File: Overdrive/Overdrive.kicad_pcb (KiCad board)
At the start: 2 copper layers, 85 x 86 mm, 53 parts, among them J1 Stereo In, J2 Barrel_Jack_Switch, J3 Mono Out, J4 M2, J5 M2, J6 M2, J7 M2, Q1 2N2222, Q2 2N2222, SW1 Footswitch, U1 RC4558

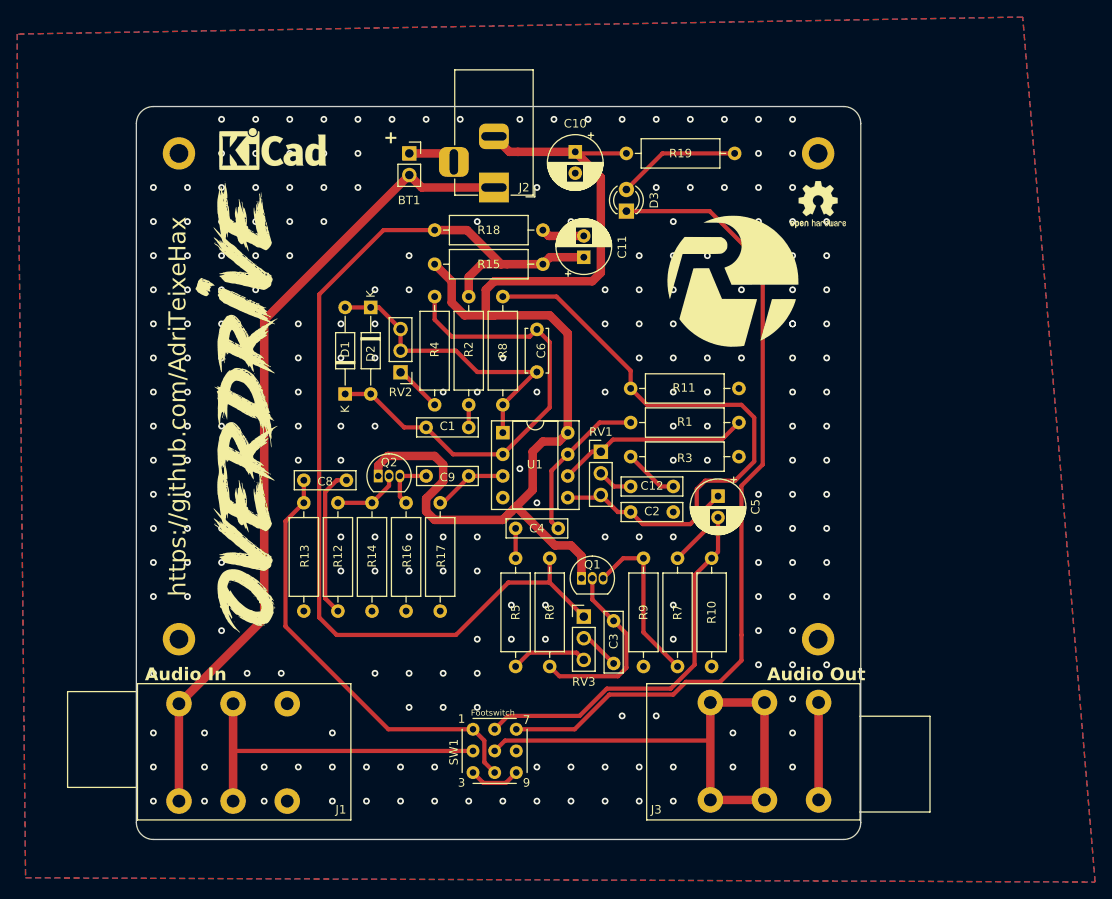
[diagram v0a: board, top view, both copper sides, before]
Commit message: Redesigned board to fit 125B case
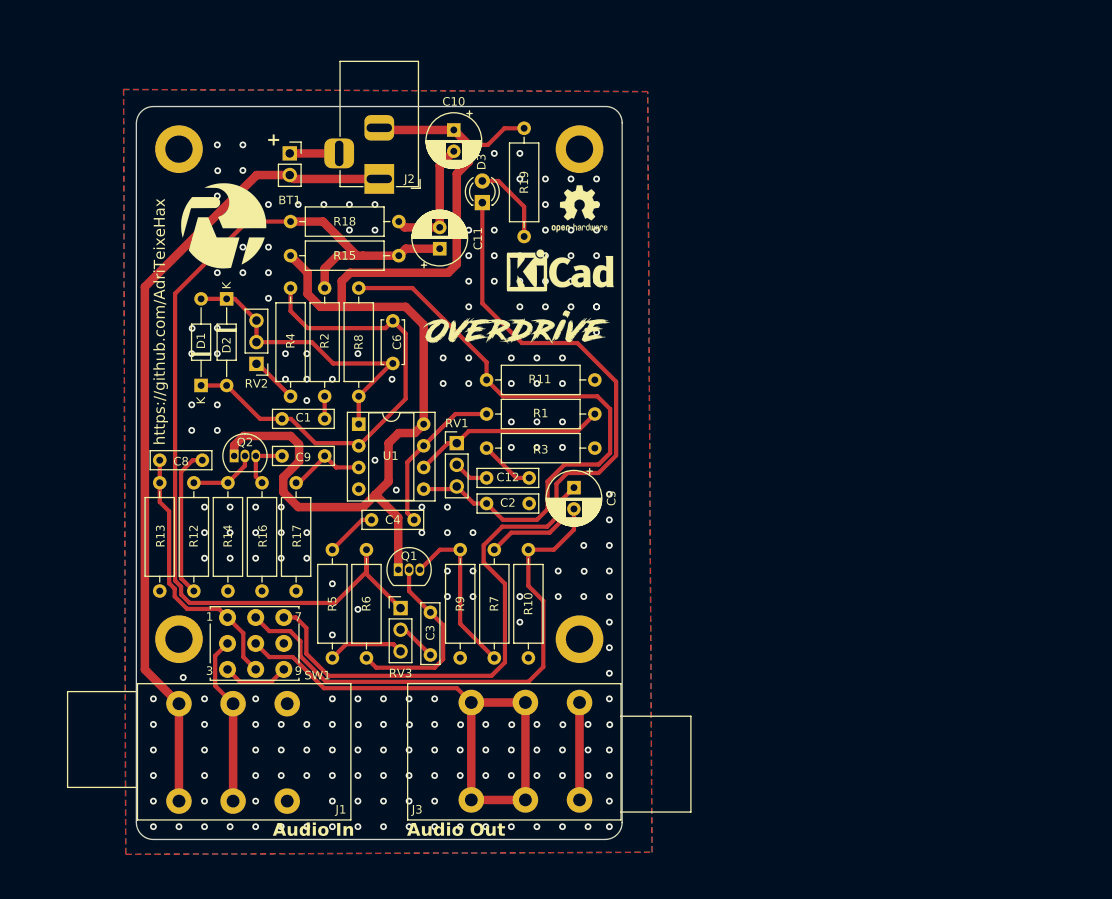
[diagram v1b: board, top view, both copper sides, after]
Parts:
- removed the G*** at (159.0, 88.0)
- removed the G*** at (104.0, 103.0)
- added G***: LOGO, LOGO, F.Cu at (99.2, 81.5)
- added G***: LOGO, LOGO, F.Cu at (133.5, 94.8)
- J4, J5, J6, J7: footprint MountingHole:MountingHole_2.2mm_M2_DIN965_Pad -> MountingHole:MountingHole_3.2mm_M3_DIN965_Pad
- moved REF** 36.6 mm to (138.8, 87.2)
- moved SW1 31.6 mm to (99.7, 127.5)
- moved J3 28.0 mm to (128.3, 137.4)
- moved J5 28.0 mm to (141.0, 72.5)
- moved REF** 28.0 mm to (141.0, 79.5)
- moved J7 28.0 mm to (141.0, 130.0)
- moved R19 26.6 mm to (134.5, 82.8), turned to 90 degrees
- moved C3 21.5 mm to (123.5, 131.8)
- moved R10 21.5 mm to (135.0, 119.5)
- moved R5 21.5 mm to (112.0, 119.5)
- moved R6 21.5 mm to (116.0, 132.2)
- moved R7 21.5 mm to (131.0, 132.2)
- moved R9 21.5 mm to (127.0, 119.5)
- moved RV3 21.5 mm to (120.0, 126.3)
- moved Q1 21.5 mm to (119.7, 121.8)
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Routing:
- net Net-(J1-PadR): track 45.1 -> 20.0 mm
- net Net-(C8-Pad1): track 51.2 -> 31.4 mm
- net Net-(C5-Pad2): track 45.0 -> 61.9 mm
- net Net-(D3-K): track 95.9 -> 108.2 mm
- net GND: track 16.5 -> 26.1 mm, vias 231 -> 216
- net +4V: track 119.7 -> 113.6 mm
- net Net-(D3-A): track 14.5 -> 9.65 mm
- net Net-(J3-PadR): track 68.3 -> 63.7 mm
- net Net-(C5-Pad1): track 9.25 -> 13.8 mm
- net +9V: track 137.1 -> 133.5 mm
- net Net-(C4-Pad2): track 3.50 -> 6.04 mm
- net Net-(SW1-Pad3): track 6.08 -> 7.81 mm
- net Net-(U1A-+): track 8.30 -> 9.36 mm
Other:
- board size 85 x 86 mm -> 57 x 86 mm

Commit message: added bom, gerber files and fixed last errors in pcb
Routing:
- net GND: track 26.1 -> 34.1 mm, vias 216 -> 225
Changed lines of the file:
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@@
       (outputformat 1)
       (mirror false)
-      (drillshape 1)
+      (drillshape 0)
       (scaleselection 1)
       (outputdirectory "")
@@
   (segment (start 130.095 99.58) (end 130.095 97.5) (width 0.5) (layer "F.Cu") (net 5))
   (segment (start 143.245 109.5) (end 144.595 108.15) (width 0.5) (layer "F.Cu") (net 5))
+  (segment (start 142.795 99.58) (end 139.42 99.58) (width 0.25) (layer "F.Cu") (net 6))
+  (segment (start 91.745 124.35) (end 91.745 120.745) (width 0.25) (layer "F.Cu") (net 6))
   (segment (start 126.25 72.75) (end 124.595 74.405) (width 1) (layer "F.Cu") (net 6))
+  (segment (start 91.745 120.745) (end 91.5 120.5) (width 0.25) (layer "F.Cu") (net 6))
   (segment (start 124.595 74.405) (end 124.595 81.682379) (width 1) (layer "F.Cu") (net 6))
   (segment (start 141 137.43) (end 141 148.86) (width 1) (layer "F.Cu") (net 6))
   (segment (start 120.477379 81.682379) (end 119.795 81) (width 1) (layer "F.Cu") (net 6))
+  (segment (start 139.42 99.58) (end 139 100) (width 0.25) (layer "F.Cu") (net 6))
   (segment (start 124.595 81.682379) (end 120.477379 81.682379) (width 1) (layer "F.Cu") (net 6))
   (via (at 124 137) (size 0.8) (drill 0.4) (layers "F.Cu" "B.Cu") (free) (net 6))
@@
   (via (at 124 149) (size 0.8) (drill 0.4) (layers "F.Cu" "B.Cu") (free) (net 6))
   (via (at 109 117.5) (size 0.8) (drill 0.4) (layers "F.Cu" "B.Cu") (free) (net 6))
+  (via (at 92.5 78) (size 0.8) (drill 0.4) (layers "F.Cu" "B.Cu") (free) (net 6))
   (via (at 138.5 122) (size 0.8) (drill 0.4) (layers "F.Cu" "B.Cu") (free) (net 6))
   (via (at 101.5 87) (size 0.8) (drill 0.4) (layers "F.Cu" "B.Cu") (free) (net 6))
@@
   (via (at 118 137) (size 0.8) (drill 0.4) (layers "F.Cu" "B.Cu") (free) (net 6))
   (via (at 139.045931 140.032175) (size 0.8) (drill 0.4) (layers "F.Cu" "B.Cu") (free) (net 6))
+  (via (at 108 69) (size 0.8) (drill 0.4) (layers "F.Cu" "B.Cu") (free) (net 6))
   (via (at 117 79) (size 0.8) (drill 0.4) (layers "F.Cu" "B.Cu") (free) (net 6))
   (via (at 91 137) (size 0.8) (drill 0.4) (layers "F.Cu" "B.Cu") (free) (net 6))
@@
   (via (at 115 152) (size 0.8) (drill 0.4) (layers "F.Cu" "B.Cu") (free) (net 6))
   (via (at 104.5 79) (size 0.8) (drill 0.4) (layers "F.Cu" "B.Cu") (free) (net 6))
-  (via (at 143 76) (size 0.8) (drill 0.4) (layers "F.Cu" "B.Cu") (free) (net 6))
+  (via (at 95.5 81) (size 0.8) (drill 0.4) (layers "F.Cu" "B.Cu") (free) (net 6))
   (via (at 112 149) (size 0.8) (drill 0.4) (layers "F.Cu" "B.Cu") (free) (net 6))
   (via (at 137 91) (size 0.8) (drill 0.4) (layers "F.Cu" "B.Cu") (free) (net 6))
   (via (at 144.5 146) (size 0.8) (drill 0.4) (layers "F.Cu" "B.Cu") (free) (net 6))
   (via (at 134 76) (size 0.8) (drill 0.4) (layers "F.Cu" "B.Cu") (free) (net 6))
+  (via (at 95.5 78) (size 0.8) (drill 0.4) (layers "F.Cu" "B.Cu") (free) (net 6))
   (via (at 103 152) (size 0.8) (drill 0.4) (layers "F.Cu" "B.Cu") (free) (net 6))
+  (via (at 91.5 120.5) (size 0.8) (drill 0.4) (layers "F.Cu" "B.Cu") (free) (net 6))
   (via (at 103 140) (size 0.8) (drill 0.4) (layers "F.Cu" "B.Cu") (free) (net 6))
   (via (at 133.045931 140.032175) (size 0.8) (drill 0.4) (layers "F.Cu" "B.Cu") (free) (net 6))
@@
   (via (at 144.5 122) (size 0.8) (drill 0.4) (layers "F.Cu" "B.Cu") (free) (net 6))
   (via (at 98.5 87) (size 0.8) (drill 0.4) (layers "F.Cu" "B.Cu") (free) (net 6))
+  (via (at 92.5 84) (size 0.8) (drill 0.4) (layers "F.Cu" "B.Cu") (free) (net 6))
   (via (at 127 143) (size 0.8) (drill 0.4) (layers "F.Cu" "B.Cu") (free) (net 6))
   (via (at 133 100) (size 0.8) (drill 0.4) (layers "F.Cu" "B.Cu") (free) (net 6))
@@
   (via (at 112 99.5) (size 0.8) (drill 0.4) (layers "F.Cu" "B.Cu") (free) (net 6))
   (via (at 109 152) (size 0.8) (drill 0.4) (layers "F.Cu" "B.Cu") (free) (net 6))
+  (via (at 101.5 69) (size 0.8) (drill 0.4) (layers "F.Cu" "B.Cu") (free) (net 6))
   (via (at 101.5 84) (size 0.8) (drill 0.4) (layers "F.Cu" "B.Cu") (free) (net 6))
   (via (at 127.045931 140.032175) (size 0.8) (drill 0.4) (layers "F.Cu" "B.Cu") (free) (net 6))
+  (via (at 111.5 69) (size 0.8) (drill 0.4) (layers "F.Cu" "B.Cu") (free) (net 6))
   (via (at 144.5 125) (size 0.8) (drill 0.4) (layers "F.Cu" "B.Cu") (free) (net 6))
   (via (at 133 107.5) (size 0.8) (drill 0.4) (layers "F.Cu" "B.Cu") (free) (net 6))
@@
   (via (at 95.5 105.5) (size 0.8) (drill 0.4) (layers "F.Cu" "B.Cu") (free) (net 6))
   (via (at 142 143) (size 0.8) (drill 0.4) (layers "F.Cu" "B.Cu") (free) (net 6))
-  (via (at 143 91) (size 0.8) (drill 0.4) (layers "F.Cu" "B.Cu") (free) (net 6))
   (via (at 139 104.5) (size 0.8) (drill 0.4) (layers "F.Cu" "B.Cu") (free) (net 6))
   (via (at 109 143) (size 0.8) (drill 0.4) (layers "F.Cu" "B.Cu") (free) (net 6))
   (via (at 103 137) (size 0.8) (drill 0.4) (layers "F.Cu" "B.Cu") (free) (net 6))
   (via (at 136 104.5) (size 0.8) (drill 0.4) (layers "F.Cu" "B.Cu") (free) (net 6))
-  (via (at 140 76) (size 0.8) (drill 0.4) (layers "F.Cu" "B.Cu") (free) (net 6))
   (via (at 144.5 119) (size 0.8) (drill 0.4) (layers "F.Cu" "B.Cu") (free) (net 6))
   (via (at 125.5 122) (size 0.8) (drill 0.4) (layers "F.Cu" "B.Cu") (free) (net 6))
@@
   (via (at 106.5 96.5) (size 0.8) (drill 0.4) (layers "F.Cu" "B.Cu") (free) (net 6))
   (via (at 111 79) (size 0.8) (drill 0.4) (layers "F.Cu" "B.Cu") (free) (net 6))
+  (via (at 92.5 81) (size 0.8) (drill 0.4) (layers "F.Cu" "B.Cu") (free) (net 6))
   (via (at 122.5 114.5) (size 0.8) (drill 0.4) (layers "F.Cu" "B.Cu") (free) (net 6))
   (via (at 144.5 131) (size 0.8) (drill 0.4) (layers "F.Cu" "B.Cu") (free) (net 6))
   (via (at 140 82) (size 0.8) (drill 0.4) (layers "F.Cu" "B.Cu") (free) (net 6))
   (via (at 128.5 117.5) (size 0.8) (drill 0.4) (layers "F.Cu" "B.Cu") (free) (net 6))
+  (via (at 98.5 69) (size 0.8) (drill 0.4) (layers "F.Cu" "B.Cu") (free) (net 6))
   (via (at 117 82) (size 0.8) (drill 0.4) (layers "F.Cu" "B.Cu") (free) (net 6))
   (via (at 115 146) (size 0.8) (drill 0.4) (layers "F.Cu" "B.Cu") (free) (net 6))
@@
   (via (at 134 128) (size 0.8) (drill 0.4) (layers "F.Cu" "B.Cu") (free) (net 6))
   (via (at 138.5 125) (size 0.8) (drill 0.4) (layers "F.Cu" "B.Cu") (free) (net 6))
+  (via (at 104.5 69) (size 0.8) (drill 0.4) (layers "F.Cu" "B.Cu") (free) (net 6))
   (via (at 136 100) (size 0.8) (drill 0.4) (layers "F.Cu" "B.Cu") (free) (net 6))
   (via (at 144.5 143) (size 0.8) (drill 0.4) (layers "F.Cu" "B.Cu") (free) (net 6))
@@
   (via (at 97 152) (size 0.8) (drill 0.4) (layers "F.Cu" "B.Cu") (free) (net 6))
   (via (at 101.5 75) (size 0.8) (drill 0.4) (layers "F.Cu" "B.Cu") (free) (net 6))
+  (via (at 104.5 72) (size 0.8) (drill 0.4) (layers "F.Cu" "B.Cu") (free) (net 6))
   (via (at 134 85) (size 0.8) (drill 0.4) (layers "F.Cu" "B.Cu") (free) (net 6))
   (via (at 124 146) (size 0.8) (drill 0.4) (layers "F.Cu" "B.Cu") (free) (net 6))

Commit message: minor changes
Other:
- board text added: "K"
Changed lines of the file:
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@@
     (property "ki_keywords" "cap capacitor")
     (attr through_hole)
-    (fp_text reference "C10" (at -3.317621 0 -180) (layer "F.SilkS")
+    (fp_text reference "C10" (at -1.67 -3.798 -180) (layer "F.SilkS")
         (effects (font (size 1 1) (thickness 0.15)))
     )
@@
     )
   )
+  (gr_text "K" (at 130.556 81.788) (layer "F.SilkS")
+    (effects (font (size 1.5 1.5) (thickness 0.3) bold) (justify left bottom))
+  )
   (gr_text "Audio In" (at 105 153.25) (layer "F.SilkS")
